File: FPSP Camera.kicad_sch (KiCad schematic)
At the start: 73 parts, among them J1 Conn_01x24_Socket, J2 Conn_01x02, J3 Conn_02x07_Counter_Clockwise, J4 Conn_02x07_Counter_Clockwise, SW1 PTS526_SM15_SMTR2_LFS, SW2 SW_Nidec_CAS-120A1, U1 LSM6DSL, U2 W25Q128JVS, U3 RP2350_60QFN, U4 TLV75533PDRV, U5 TLV73328PDRV, U6 TLV73315PDRV, Y1 SiT8008xx-1x-xxE

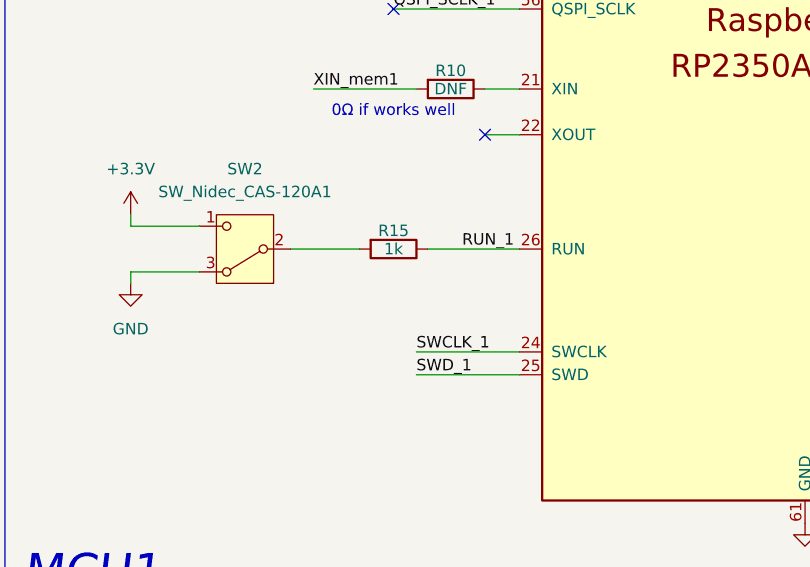
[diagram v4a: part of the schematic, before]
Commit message: connector board pin order updated
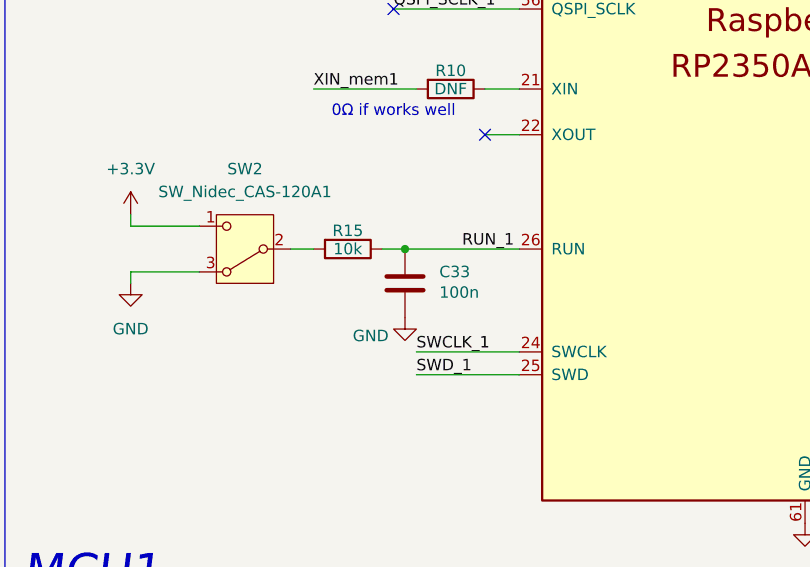
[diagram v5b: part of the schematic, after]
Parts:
- added C33: 100n, Capacitor_SMD:C_0402_1005Metric, symbol Device:C
- R15: value 1k -> 10k
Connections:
- net GND: now also C33.2
- net RUN_1: now also C33.1
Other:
- moved on the sheet: R15

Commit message: new connector footprint updated
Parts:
- removed J3, J4: Conn_02x07_Counter_Clockwise, Connector_Molex:Molex_SlimStack_502426-1410_2x07_P0.40mm_Vertical, symbol Connector_Generic:Conn_02x07_Odd_Even
- added J4, J5: Conn_02x06_Top_Bottom, 5035481222:CON_5035481222, symbol Connector_Generic:Conn_02x06_Top_Bottom
- renumbered C33 to C24, C24 to C25, C25 to C26, C26 to C27, C27 to C28, C28 to C29, C29 to C30, C30 to C31, C31 to C32, C32 to C33
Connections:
- net FPGA_CTRL: now also J4.1 (Pin_1)
- net FPGA_EN: now also J4.6 (Pin_6)
- net GND: now also J4.12 (Pin_12), J5.12 (Pin_12)
- net HREF_OUT: now also J4.7 (Pin_7)
- net IMAGE_CLK: now also J4.8 (Pin_8)
- net IMAGE_OUT_1: now also J4.5 (Pin_5)
- net IMAGE_OUT_2: now also J4.4 (Pin_4)
- net IMAGE_OUT_3: now also J4.3 (Pin_3)
- net IMAGE_OUT_4: now also J4.2 (Pin_2)
- net POSITION_OUT_1: now also J4.11 (Pin_11)
- net POSITION_OUT_CLK: now also J4.10 (Pin_10)
- net SWCLK_1: now also J5.3 (Pin_3)
- net SWD_1: now also J5.4 (Pin_4)
- net USB_D1+: now also J5.1 (Pin_1)
- net USB_D1-: now also J5.2 (Pin_2)
- net VSYNC_OUT: now also J4.9 (Pin_9)
- no-connect marks 22 -> 18

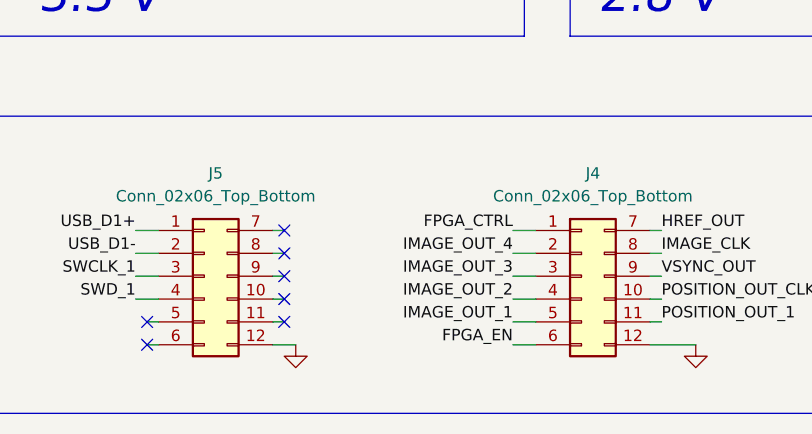
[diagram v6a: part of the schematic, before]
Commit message: connector footprint swapped
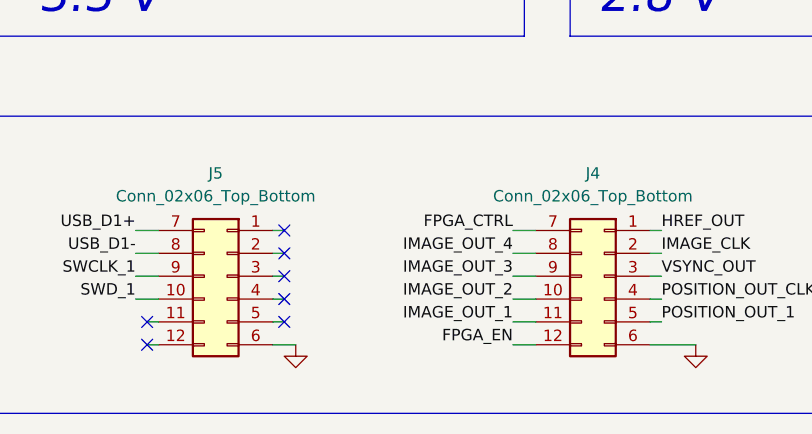
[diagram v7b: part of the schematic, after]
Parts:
- J4, J5: footprint 5035481222:CON_5035481222 -> 5035521222:CON_5035521222
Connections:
- net FPGA_CTRL: now also J4.7 (Pin_7); no longer J4.1 (Pin_1)
- net FPGA_EN: now also J4.12 (Pin_12); no longer J4.6 (Pin_6)
- net GND: now also J4.6 (Pin_6), J5.6 (Pin_6); no longer J4.12 (Pin_12), J5.12 (Pin_12)
- net HREF_OUT: now also J4.1 (Pin_1); no longer J4.7 (Pin_7)
- net IMAGE_CLK: now also J4.2 (Pin_2); no longer J4.8 (Pin_8)
- net IMAGE_OUT_1: now also J4.11 (Pin_11); no longer J4.5 (Pin_5)
- net IMAGE_OUT_2: now also J4.10 (Pin_10); no longer J4.4 (Pin_4)
- net IMAGE_OUT_3: now also J4.9 (Pin_9); no longer J4.3 (Pin_3)
- net IMAGE_OUT_4: now also J4.8 (Pin_8); no longer J4.2 (Pin_2)
- net POSITION_OUT_1: now also J4.5 (Pin_5); no longer J4.11 (Pin_11)
- net POSITION_OUT_CLK: now also J4.4 (Pin_4); no longer J4.10 (Pin_10)
- net SWCLK_1: now also J5.9 (Pin_9); no longer J5.3 (Pin_3)
- net SWD_1: now also J5.10 (Pin_10); no longer J5.4 (Pin_4)
- net USB_D1+: now also J5.7 (Pin_7); no longer J5.1 (Pin_1)
- net USB_D1-: now also J5.8 (Pin_8); no longer J5.2 (Pin_2)
- net VSYNC_OUT: now also J4.3 (Pin_3); no longer J4.9 (Pin_9)
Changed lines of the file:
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@@
 	)
 	(symbol
+		(lib_id "Connector_Generic:Conn_02x06_Top_Bottom")
+		(at 92.71 260.35 0)
+		(mirror y)
+		(unit 1)
+		(body_style 1)
+		(exclude_from_sim no)
+		(in_bom yes)
+		(on_board yes)
+		(in_pos_files yes)
+		(dnp no)
+		(property "Reference" "J4"
+			(at 91.44 248.92 0)
+			(show_name no)
+			(do_not_autoplace no)
+			(effects
+				(font
+					(size 1.27 1.27)
+				)
+			)
+		)
+		(property "Value" "Conn_02x06_Top_Bottom"
+			(at 91.44 251.46 0)
+			(show_name no)
+			(do_not_autoplace no)
+			(effects
+				(font
+					(size 1.27 1.27)
+				)
+			)
+		)
+		(property "Footprint" "5035521222:CON_5035521222"
+			(at 92.71 260.35 0)
+			(hide yes)
+			(show_name no)
+			(do_not_autoplace no)
+			(effects
+				(font
+					(size 1.27 1.27)
+				)
+			)
+		)
+		(property "Datasheet" ""
+			(at 92.71 260.35 0)
+			(hide yes)
+			(show_name no)
+			(do_not_autoplace no)
+			(effects
+				(font
+					(size 1.27 1.27)
+				)
+			)
+		)
+		(property "Description" "Generic connector, double row, 02x06, top/bottom pin numbering scheme (row 1: 1...pins_per_row, row2: pins_per_row+1 ... num_pins), script generated (kicad-library-utils/schlib/autogen/connector/)"
+			(at 92.71 260.35 0)
+			(hide yes)
+			(show_name no)
+			(do_not_autoplace no)
+			(effects
+				(font
+					(size 1.27 1.27)
+				)
+			)
+		)
+		(pin "1"
+		)
+		(pin "3"
+		)
+		(pin "5"
+		)
+		(pin "10"
+		)
+		(pin "9"
+		)
+		(pin "11"
+		)
+		(pin "6"
+		)
+		(pin "7"
+		)
+		(pin "4"
+		)
+		(pin "2"
+		)
+		(pin "8"
+		)
+		(pin "12"
+		)
+		(instances
+			(project "FPSP Camera"
+				(path "/b8279e3f-7ea4-46f5-abf2-a9173e16562f"
+					(reference "J4")
+					(unit 1)
+				)
+			)
+		)
+	)
+	(symbol
 		(lib_id "power:+1V1")
 		(at 48.26 76.2 0)
@@
 	)
 	(symbol
-		(lib_id "Connector_Generic:Conn_02x06_Top_Bottom")
-		(at 48.26 260.35 0)
-		(unit 1)
-		(body_style 1)
-		(exclude_from_sim no)
-		(in_bom yes)
-		(on_board yes)
-		(in_pos_files yes)
-		(dnp no)
-		(fields_autoplaced yes)
-		(property "Reference" "J5"
-			(at 49.53 248.92 0)
-			(show_name no)
-			(do_not_autoplace no)
-			(effects
-				(font
-					(size 1.27 1.27)
-				)
-			)
-		)
-		(property "Value" "Conn_02x06_Top_Bottom"
-			(at 49.53 251.46 0)
-			(show_name no)
-			(do_not_autoplace no)
-			(effects
-				(font
-					(size 1.27 1.27)
-				)
-			)
-		)
-		(property "Footprint" "5035481222:CON_5035481222"
-			(at 48.26 260.35 0)
-			(hide yes)
-			(show_name no)
-			(do_not_autoplace no)
-			(effects
-				(font
-					(size 1.27 1.27)
-				)
-			)
-		)
-		(property "Datasheet" ""
-			(at 48.26 260.35 0)
-			(hide yes)
-			(show_name no)
-			(do_not_autoplace no)
-			(effects
-				(font
-					(size 1.27 1.27)
-				)
-			)
-		)
-		(property "Description" "Generic connector, double row, 02x06, top/bottom pin numbering scheme (row 1: 1...pins_per_row, row2: pins_per_row+1 ... num_pins), script generated (kicad-library-utils/schlib/autogen/connector/)"
-			(at 48.26 260.35 0)
-			(hide yes)
-			(show_name no)
-			(do_not_autoplace no)
-			(effects
-				(font
-					(size 1.27 1.27)
-				)
-			)
-		)
-		(pin "1"
-		)
-		(pin "3"
-		)
-		(pin "5"
-		)
-		(pin "10"
-		)
-		(pin "9"
-		)
-		(pin "11"
-		)
-		(pin "6"
-		)
-		(pin "7"
-		)
-		(pin "4"
-		)
-		(pin "2"
-		)
-		(pin "8"
-		)
-		(pin "12"
-		)
-		(instances
-			(project "FPSP Camera"
-				(path "/b8279e3f-7ea4-46f5-abf2-a9173e16562f"
-					(reference "J5")
-					(unit 1)
-				)
-			)
-		)
-	)
-	(symbol
 		(lib_id "Device:R")
 		(at 285.75 67.31 270)
@@
 	)
 	(symbol
+		(lib_id "Connector_Generic:Conn_02x06_Top_Bottom")
+		(at 50.8 260.35 0)
+		(mirror y)
+		(unit 1)
+		(body_style 1)
+		(exclude_from_sim no)
+		(in_bom yes)
+		(on_board yes)
+		(in_pos_files yes)
+		(dnp no)
+		(property "Reference" "J5"
+			(at 49.53 248.92 0)
+			(show_name no)
+			(do_not_autoplace no)
+			(effects
+				(font
+					(size 1.27 1.27)
+				)
+			)
+		)
+		(property "Value" "Conn_02x06_Top_Bottom"
+			(at 49.53 251.46 0)
+			(show_name no)
+			(do_not_autoplace no)
+			(effects
+				(font
+					(size 1.27 1.27)
+				)
+			)
+		)
+		(property "Footprint" "5035521222:CON_5035521222"
+			(at 50.8 260.35 0)
+			(hide yes)
+			(show_name no)
+			(do_not_autoplace no)
+			(effects
+				(font
+					(size 1.27 1.27)
+				)
+			)
+		)
+		(property "Datasheet" ""
+			(at 50.8 260.35 0)
+			(hide yes)
+			(show_name no)
+			(do_not_autoplace no)
+			(effects
+				(font
+					(size 1.27 1.27)
+				)
+			)
+		)
+		(property "Description" "Generic connector, double row, 02x06, top/bottom pin numbering scheme (row 1: 1...pins_per_row, row2: pins_per_row+1 ... num_pins), script generated (kicad-library-utils/schlib/autogen/connector/)"
+			(at 50.8 260.35 0)
+			(hide yes)
+			(show_name no)
+			(do_not_autoplace no)
+			(effects
+				(font
+					(size 1.27 1.27)
+				)
+			)
+		)
+		(pin "1"
+		)
+		(pin "3"
+		)
+		(pin "5"
+		)
+		(pin "10"
+		)
+		(pin "9"
+		)
+		(pin "11"
+		)
+		(pin "6"
+		)
+		(pin "7"
+		)
+		(pin "4"
+		)
+		(pin "2"
+		)
+		(pin "8"
+		)
+		(pin "12"
+		)
+		(instances
+			(project "FPSP Camera"
+				(path "/b8279e3f-7ea4-46f5-abf2-a9173e16562f"
+					(reference "J5")
+					(unit 1)
+				)
+			)
+		)
+	)
+	(symbol
 		(lib_id "power:+1V5")
 		(at 289.56 123.19 0)
@@
 					(unit 1)
 				)
-			)
-		)
-	)
-	(symbol
-		(lib_id "Connector_Generic:Conn_02x06_Top_Bottom")
-		(at 90.17 260.35 0)
-		(unit 1)
-		(body_style 1)
-		(exclude_from_sim no)
-		(in_bom yes)
-		(on_board yes)
-		(in_pos_files yes)
-		(dnp no)
-		(fields_autoplaced yes)
-		(property "Reference" "J4"
-			(at 91.44 248.92 0)
-			(show_name no)
-			(do_not_autoplace no)
-			(effects
-				(font
-					(size 1.27 1.27)
-				)
-			)
-		)
-		(property "Value" "Conn_02x06_Top_Bottom"
-			(at 91.44 251.46 0)
-			(show_name no)
-			(do_not_autoplace no)
-			(effects
-				(font
-					(size 1.27 1.27)
-				)
-			)
-		)
-		(property "Footprint" "5035481222:CON_5035481222"
-			(at 90.17 260.35 0)
-			(hide yes)
-			(show_name no)
-			(do_not_autoplace no)
-			(effects
-				(font
-					(size 1.27 1.27)
-				)
-			)
-		)
-		(property "Datasheet" ""
-			(at 90.17 260.35 0)
-			(hide yes)
-			(show_name no)
-			(do_not_autoplace no)
-			(effects
-				(font
-					(size 1.27 1.27)
-				)
-			)
-		)
-		(property "Description" "Generic connector, double row, 02x06, top/bottom pin numbering scheme (row 1: 1...pins_per_row, row2: pins_per_row+1 ... num_pins), script generated (kicad-library-utils/schlib/autogen/connector/)"
-			(at 90.17 260.35 0)
-			(hide yes)
-			(show_name no)
-			(do_not_autoplace no)
-			(effects
-				(font
-					(size 1.27 1.27)
-				)
-			)
-		)
-		(pin "1"
-		)
-		(pin "3"
-		)
-		(pin "5"
-		)
-		(pin "10"
-		)
-		(pin "9"
-		)
-		(pin "11"
-		)
-		(pin "6"
-		)
-		(pin "7"
-		)
-		(pin "4"
-		)
-		(pin "2"
-		)
-		(pin "8"
-		)
-		(pin "12"
-		)
-		(instances
-			(project "FPSP Camera"
-				(path "/b8279e3f-7ea4-46f5-abf2-a9173e16562f"
-					(reference "J4")
-					(unit 1)
-				)

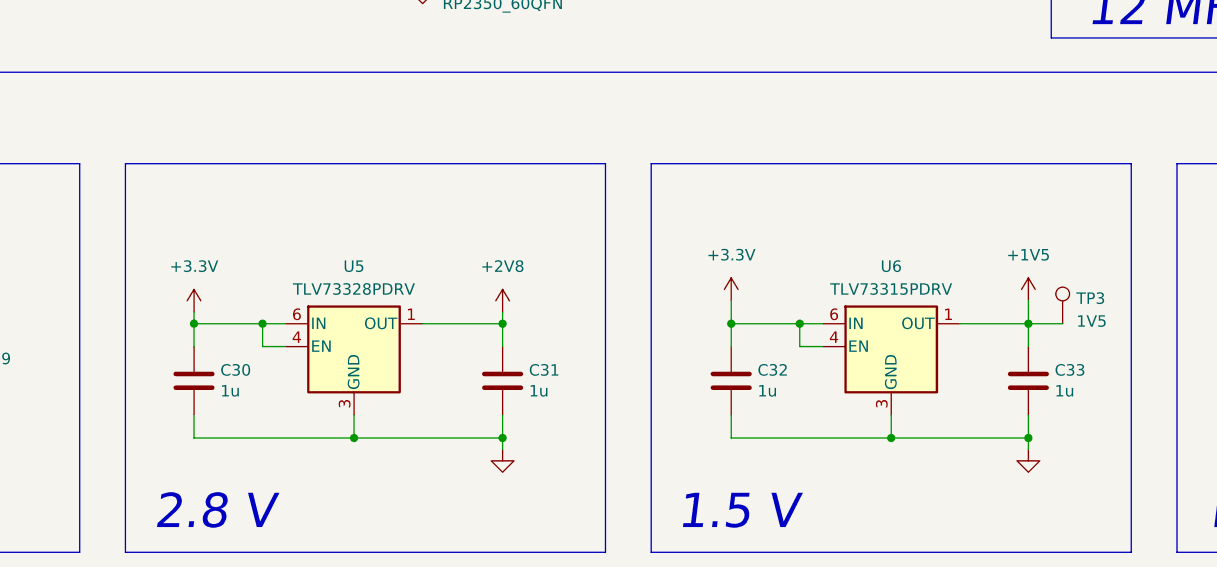
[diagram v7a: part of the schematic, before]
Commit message: LDOs replaced
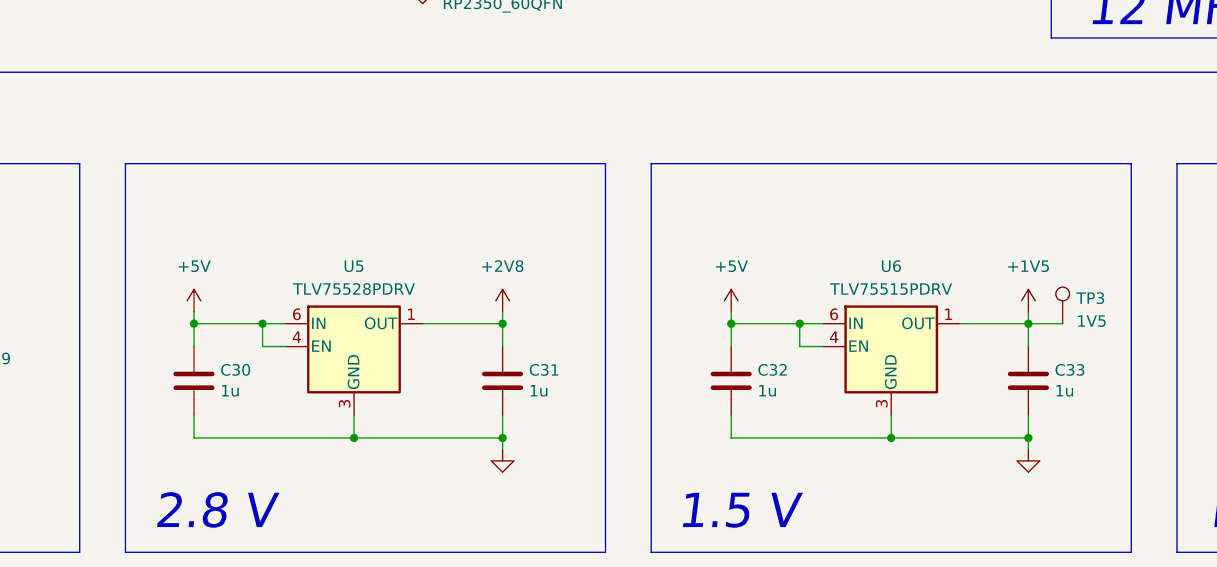
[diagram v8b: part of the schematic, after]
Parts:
- removed U5: TLV73328PDRV, Package_SON:WSON-6-1EP_2x2mm_P0.65mm_EP1x1.6mm, symbol Regulator_Linear:TLV75533PDRV
- removed U6: TLV73315PDRV, Package_SON:WSON-6-1EP_2x2mm_P0.65mm_EP1x1.6mm, symbol Regulator_Linear:TLV75533PDRV
- added U5: TLV75528PDRV, Package_SON:WSON-6-1EP_2x2mm_P0.65mm_EP1x1.6mm, symbol Regulator_Linear:TLV75528PDRV
- added U6: TLV75515PDRV, Package_SON:WSON-6-1EP_2x2mm_P0.65mm_EP1x1.6mm, symbol Regulator_Linear:TLV75515PDRV
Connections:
- net +1V5: now also U6.1 (OUT)
- net +2V8: now also U5.1 (OUT)
- net +3.3V: no longer C30.1, C32.1
- net +5V: now also C30.1, C32.1, U5.4 (EN), U5.6 (IN), U6.4 (EN), U6.6 (IN)
- net GND: now also U5.3 (GND), U5.7 (GND), U6.3 (GND), U6.7 (GND)
